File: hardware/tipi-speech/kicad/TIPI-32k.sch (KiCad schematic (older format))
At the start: 33 parts, among them J1 TI-99_Sideport, J2 USB_B_Micro, J3 Conn_01x02, P1 TI-99_Sideport, Q1 NPN_BCE, U1 XC95144XL-TQ100, U2 27C256, U3 74HCT245, U4 LM1117-3.3, U5 AS6C62256-55PCN

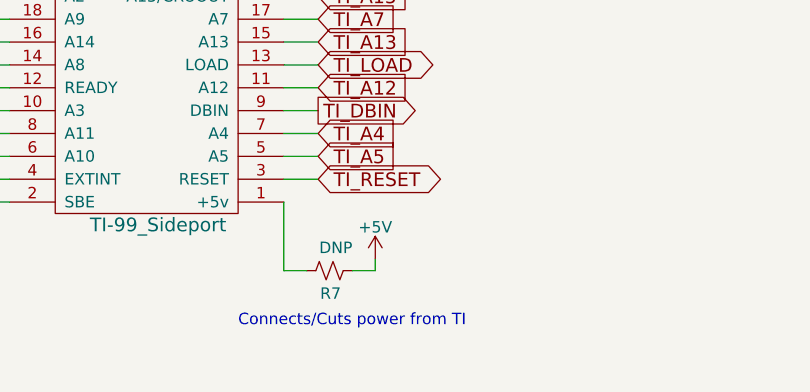
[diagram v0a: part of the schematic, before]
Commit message: TIPI/32K V2 PCB and V3 CPLD updates
This update is PCB manufacturability improvements (Via to trace increase and R7 moved to topside) and V3 CPLD changes to support RAM disable without CRU Address changes.
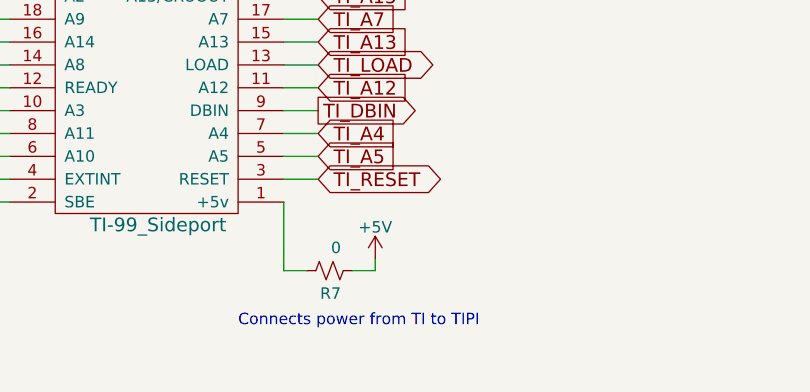
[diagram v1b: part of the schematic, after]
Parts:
- R7: value DNP -> 0
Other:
- note added: "Connects power from TI to TIPI"
- note removed: "Connects/Cuts power from TI"
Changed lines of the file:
@@
 encoding utf-8
 Sheet 1 1
-Title "SS-TIPI - TI-99/4A to RPi adapter for Speech Synth. Case"
-Date "2020-05-09"
-Rev "V1"
+Title "TIPI-32k - TI-99/4A to RPi adapter for Speech Synth. Case"
+Date "2020-06-12"
+Rev "V2"
 Comp "J-Data "
 Comment1 "github.com/jedimatt42/tipi"
@@
 P 6800 8450
 F 0 "R7" V 6700 8400 50  0000 L CNN
-F 1 "DNP" V 6900 8350 50  0000 L CNN
+F 1 "0" V 6900 8400 50  0000 L CNN
 F 2 "VS-TIPI-kicad:C_0805_HandSoldering" H 6800 8450 50  0001 C CNN
 F 3 "" H 6800 8450 50  0001 C CNN
@@
 Expansion Port out to Peripherals
 Text Notes 6400 8700 0    50   ~ 0
-Connects/Cuts power from TI
+Connects power from TI to TIPI
 Text Notes 1950 1350 0    50   ~ 0
 TIPI EPROM
